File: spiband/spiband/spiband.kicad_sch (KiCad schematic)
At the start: 18 parts, among them J1 RJ45_Shielded, U1 MAX3485, U2 MAX3485, U3 MAX3485, U4 MAX3232, U5 LM78M05_TO220, U6 TLV70018_SOT353

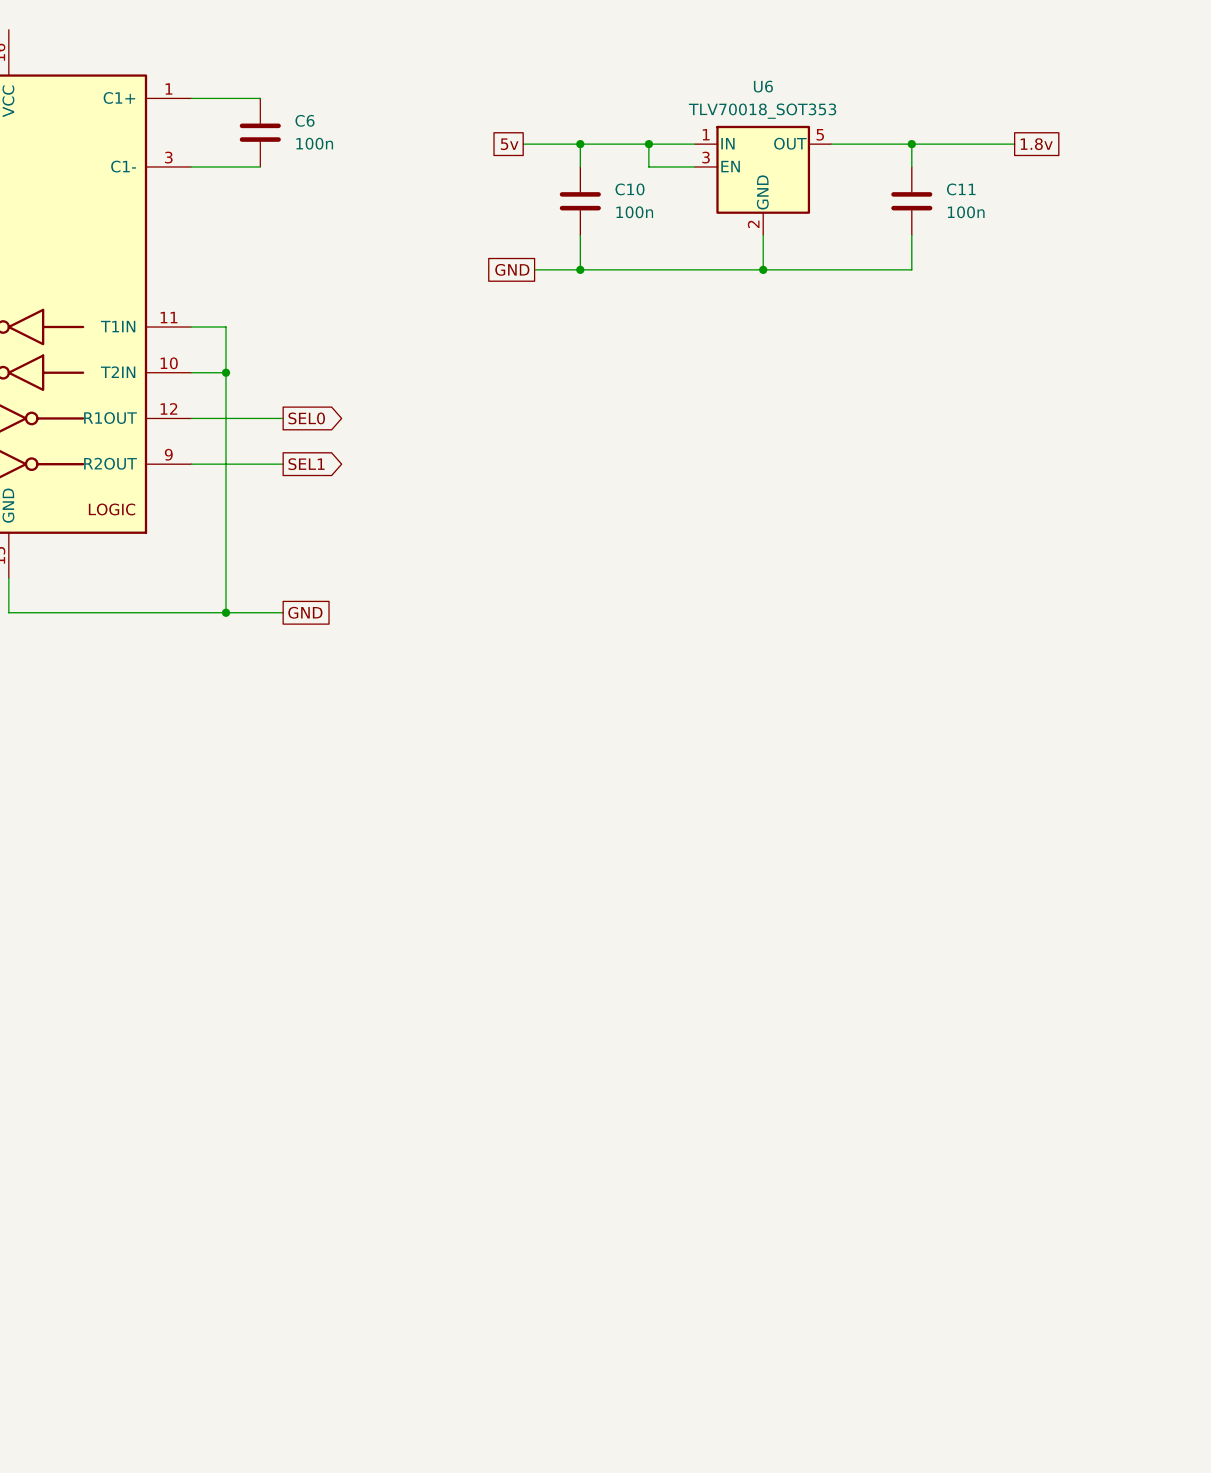
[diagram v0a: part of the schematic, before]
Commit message: Added channel schematic
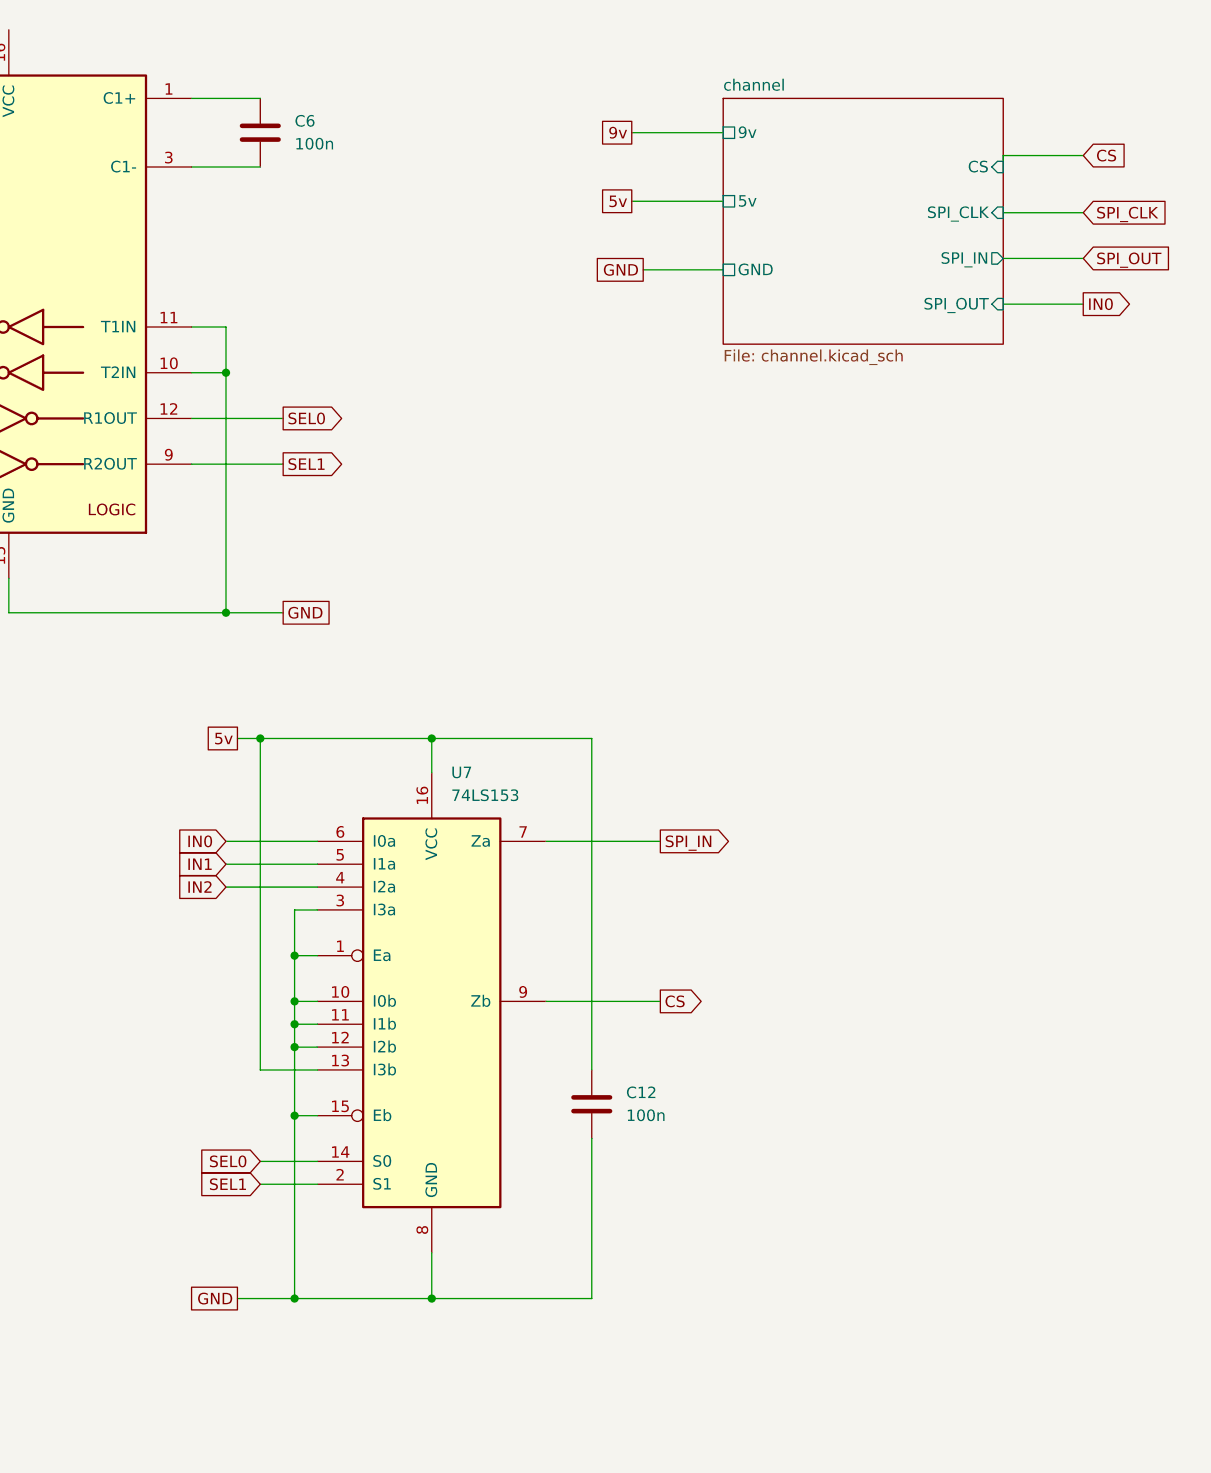
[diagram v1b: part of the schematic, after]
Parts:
- removed C10, C11: 100n, Capacitor_THT:C_Disc_D4.3mm_W1.9mm_P5.00m, symbol Device:C
- removed U6: TLV70018_SOT353, Package_TO_SOT_SMD:SOT-353_SC-70-5, symbol Regulator_Linear:TLV70018_SOT353
- added C12: 100n, Capacitor_THT:C_Disc_D4.3mm_W1.9mm_P5.00m, symbol Device:C
- added U7: 74LS153, Package_SO:SOIC-16_3.9x9.9mm_P1.27mm, symbol 74xx:74LS153
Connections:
- net 5v: now also C12.1, U7.13 (I3b), U7.16 (VCC)
- net GND: now also C12.2, U7.1 (Ea), U7.10 (I0b), U7.11 (I1b), U7.12 (I2b), U7.15 (Eb), U7.3 (I3a), U7.8 (GND)
- net SEL0: now also U7.14 (S0)
- net SEL1: now also U7.2 (S1)
- net SPI_IN: now also U7.7 (Za)
- new net CS: U7.9 (Zb)
- new net IN0: U7.6 (I0a)
- new net IN1: U7.5 (I1a)
- new net IN2: U7.4 (I2a)
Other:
- added sheet channel (channel.kicad_sch)

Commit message: SPI band schema done.
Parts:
- added C10: 100n, Capacitor_THT:C_Disc_D4.3mm_W1.9mm_P5.00mm, symbol Device:C
- added C11: 100n, Capacitor_SMD:C_0805_2012Metric_Pad1.18x1.45mm_HandSolder, symbol Device:C
- added U6: TLV70018_SOT353, Package_TO_SOT_SMD:SOT-353_SC-70-5, symbol Regulator_Linear:TLV70018_SOT353
- C1, C12, C3, C4, C5, C6, C7, C8, C9: footprint Capacitor_THT:C_Disc_D4.3mm_W1.9mm_P5.00m -> Capacitor_SMD:C_0805_2012Metric_Pad1.18x1.45mm_HandSolder
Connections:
- net 5v: now also C10.1, U6.1 (IN), U6.3 (EN)
- net GND: now also C10.2, C11.2, U6.2 (GND)
- new net 1.8v: C11.1, U6.5 (OUT)
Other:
- removed sheet channel
- added sheet Channel0 (channel.kicad_sch)
- added sheet Channel1 (channel.kicad_sch)
- added sheet Channel2 (channel.kicad_sch)

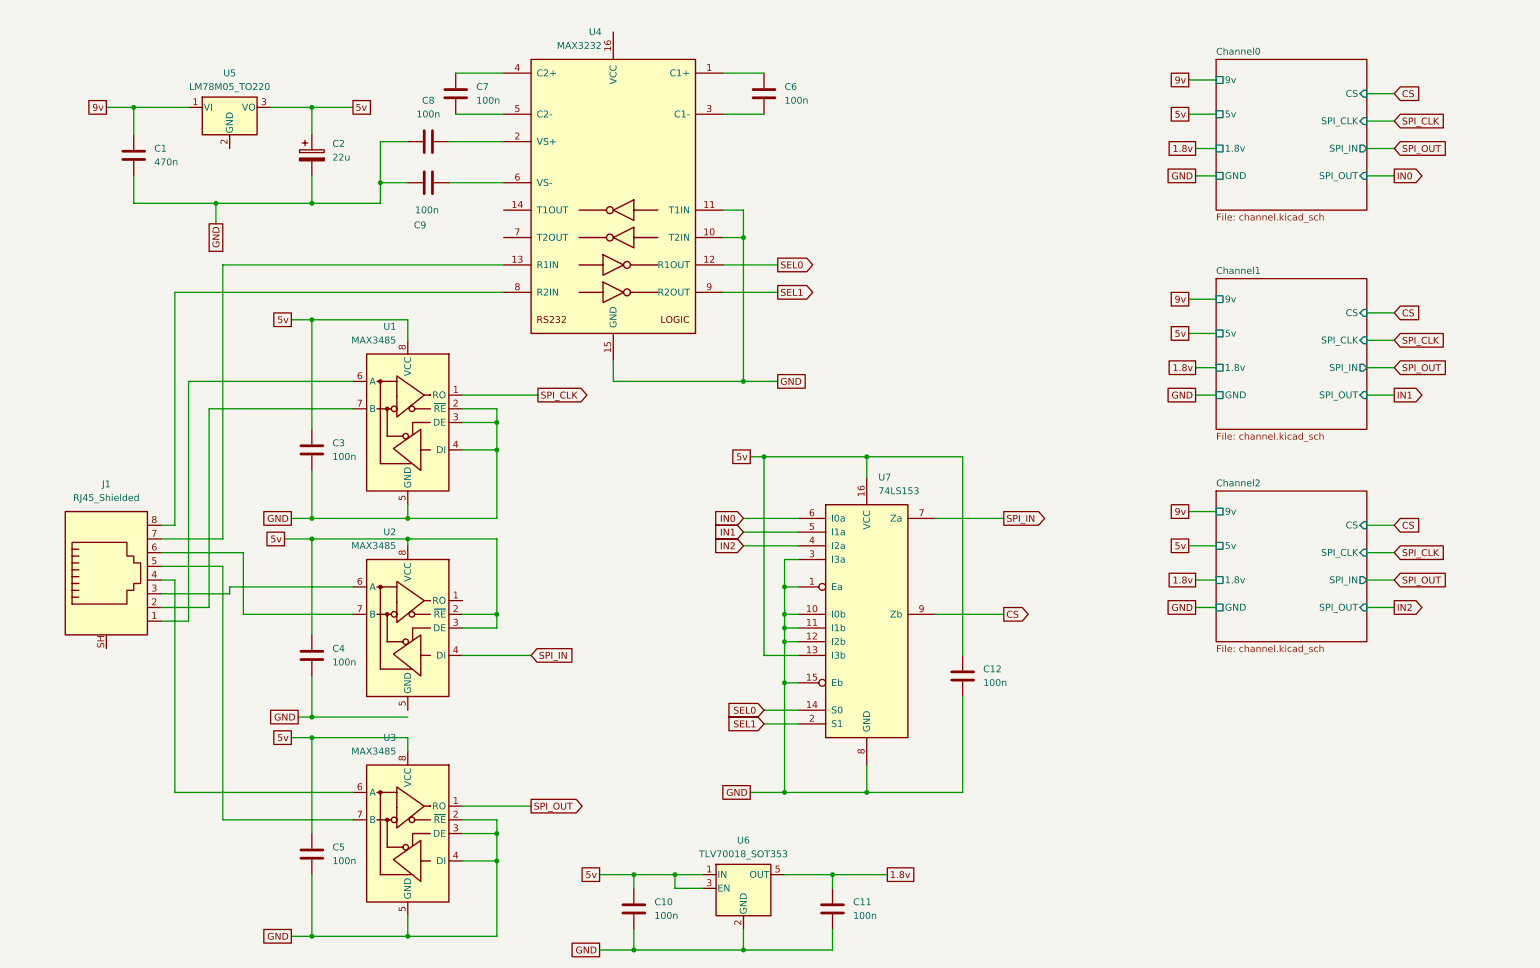
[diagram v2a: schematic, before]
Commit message: Changed to 3.3v supply voltage.
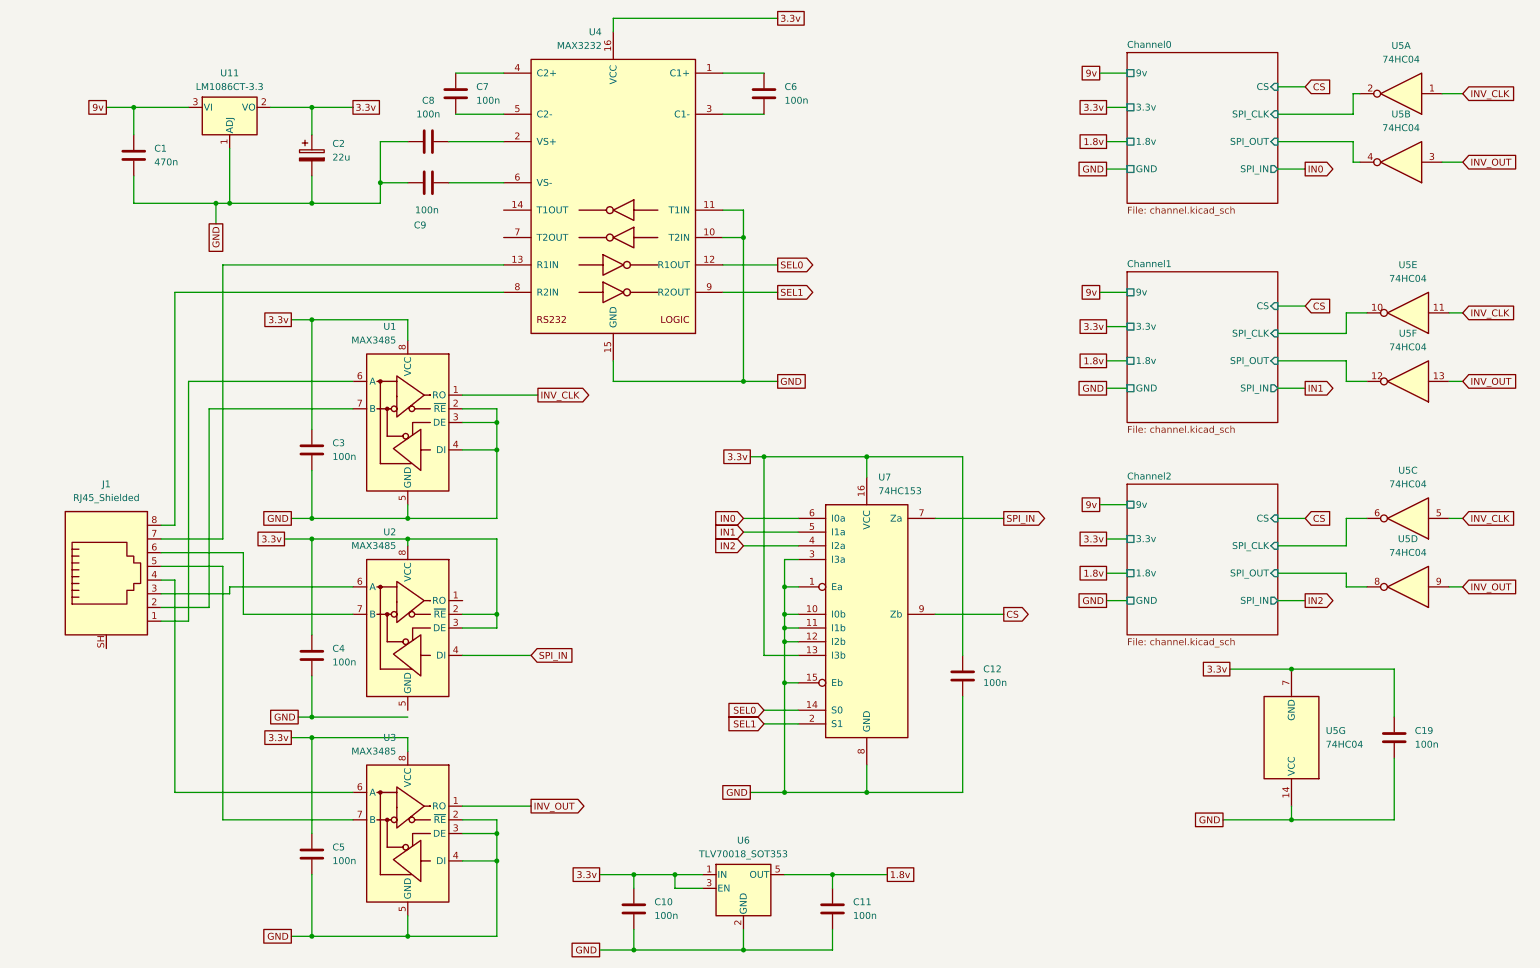
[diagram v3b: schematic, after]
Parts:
- removed U5: LM78M05_TO220, Package_TO_SOT_THT:TO-220-3_Horizontal_TabDown, symbol Regulator_Linear:LM78M05_TO220
- added C19: 100n, Capacitor_SMD:C_0805_2012Metric_Pad1.18x1.45mm_HandSolder, symbol Device:C
- added U11: LM1086CT-3.3, Package_TO_SOT_THT:TO-220-3_Horizontal_TabDown, symbol Regulator_Linear:LM317_TO-220
- added U5: 74HC04, Package_SO:SOIC-14_3.9x8.7mm_P1.27mm, symbol 74xx:74LS04
- U7: value 74LS153 -> 74HC153
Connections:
- net 5v is gone; now on net 3.3v: C10.1, C12.1, C2.1, C3.1, C4.1, C5.1, U1.8 (VCC), U2.2 (~{RE}), U2.3 (DE), U2.8 (VCC), U3.8 (VCC), U6.1 (IN), U6.3 (EN), U7.13 (I3b), U7.16 (VCC)
- net 9v: now also U11.3 (VI)
- net GND: now also C19.2, U11.1 (ADJ), U5.14 (VCC)
- net 3.3v: now reaches U4.16 (VCC)
- net 3.3v: now also C19.1, U11.2 (VO), U5.7 (GND)
- net SPI_CLK renamed INV_CLK
- net INV_CLK: now also U5.1, U5.11, U5.5
- net SPI_OUT renamed INV_OUT
- net INV_OUT: now also U5.13, U5.3, U5.9
- new net Channel0/SPI_CLK: U5.2
- new net Channel0/SPI_OUT: U5.4
- new net Channel1/SPI_CLK: U5.10
- new net Channel1/SPI_OUT: U5.12
- new net Channel2/SPI_CLK: U5.6
- new net Channel2/SPI_OUT: U5.8
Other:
- sheet Channel0 ports: added 3.3v; removed 5v
- sheet Channel1 ports: added 3.3v; removed 5v
- sheet Channel2 ports: added 3.3v; removed 5v

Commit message: Finalized SPI interface PCB
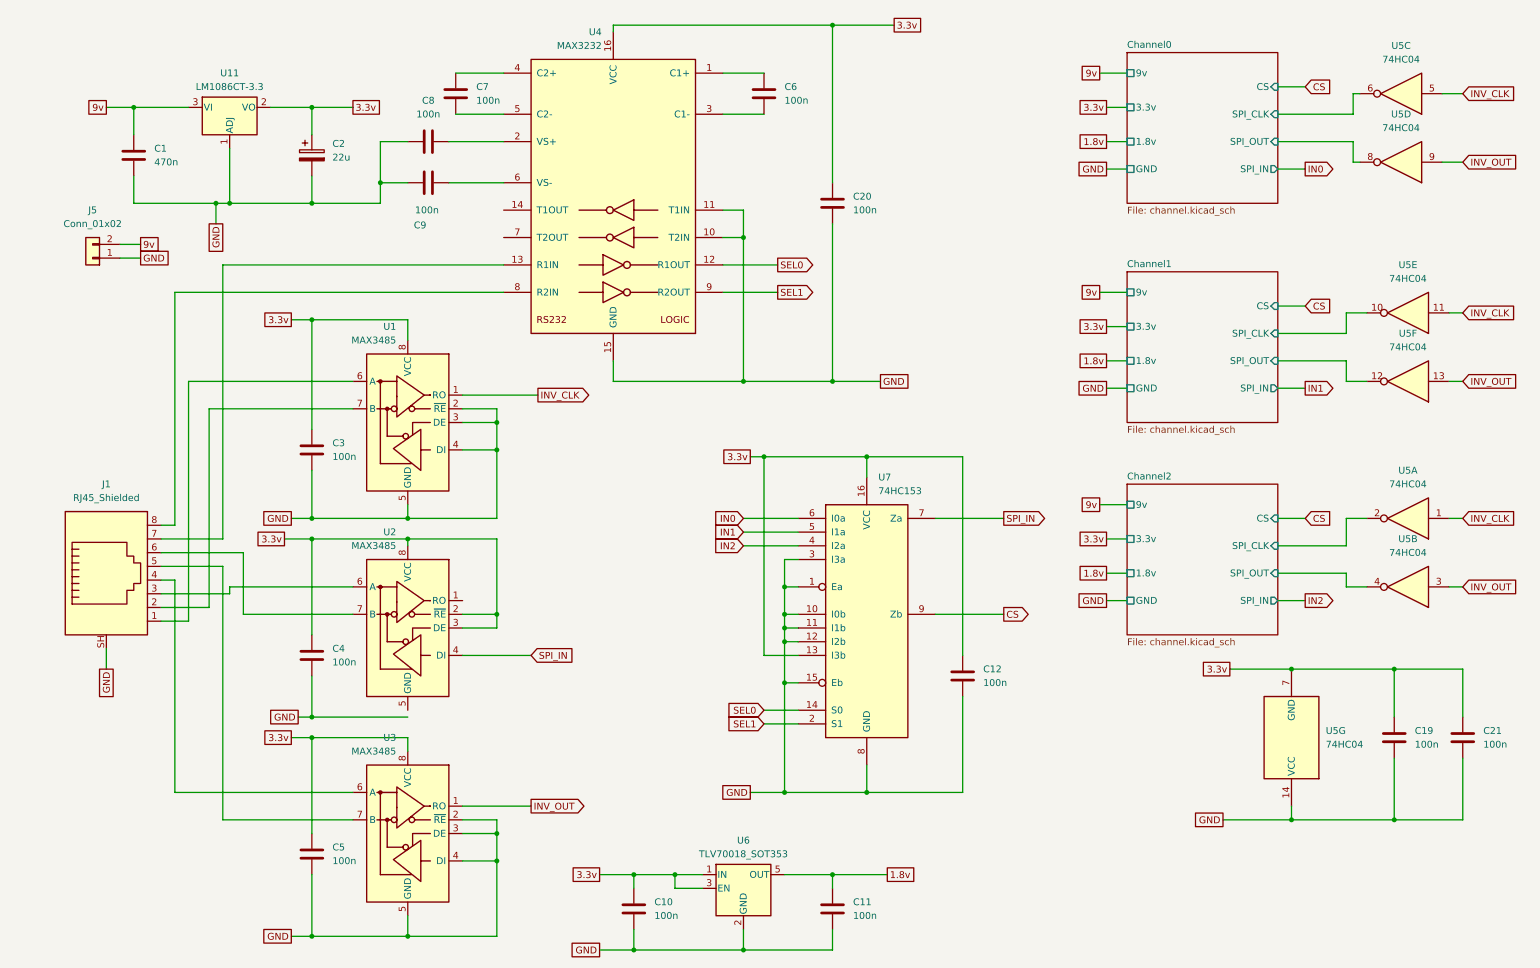
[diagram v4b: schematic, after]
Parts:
- added C20, C21: 100n, Capacitor_SMD:C_0805_2012Metric_Pad1.18x1.45mm_HandSolder, symbol Device:C
- added J5: Conn_01x02, Connector_PinHeader_2.54mm:PinHeader_1x02_P2.54mm_Vertical, symbol Connector_Generic:Conn_01x02
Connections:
- net 3.3v: now also C20.1, C21.1
- net 9v: now also J5.2 (Pin_2)
- net Channel0/SPI_CLK: now also U5.6; no longer U5.2
- net Channel0/SPI_OUT: now also U5.8; no longer U5.4
- net Channel2/SPI_CLK: now also U5.2; no longer U5.6
- net Channel2/SPI_OUT: now also U5.4; no longer U5.8
- net GND: now also J1.SH, C20.2, C21.2, J5.1 (Pin_1)
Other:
- moved on the sheet: U5A, U5B, U5C, U5D
